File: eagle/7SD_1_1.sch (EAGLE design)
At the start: 16 parts, among them P1 7-SEG_SA56-11, X1 In A, X2 In B

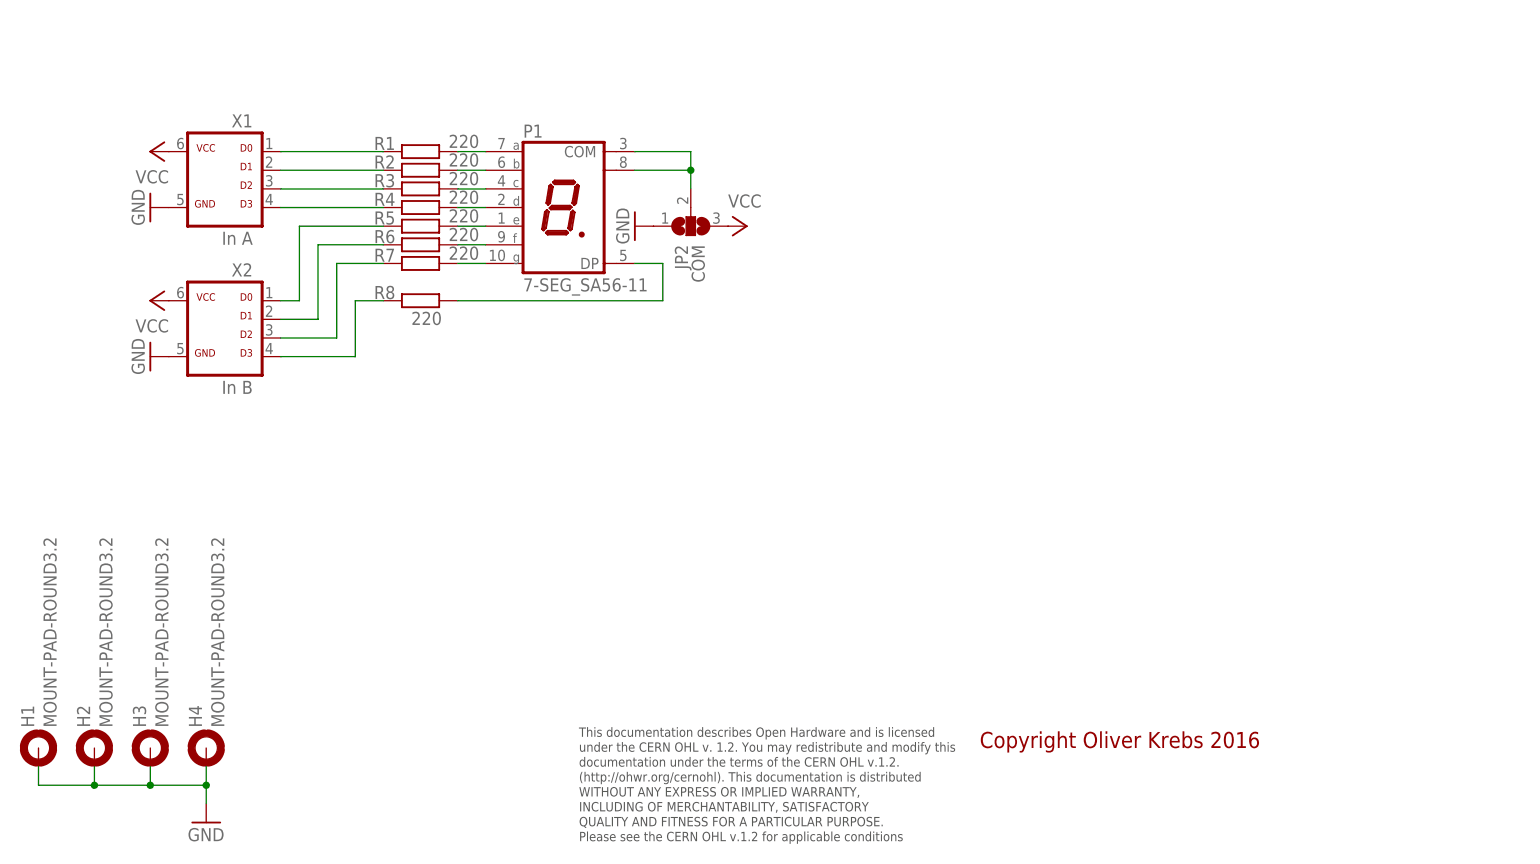
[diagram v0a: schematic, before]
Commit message: Add new tetra-Board and arduino files
Add AMP_1_0, AVC_1_0, D18_1_1, IOP_1_2, MIC_1_0, PIN_1_1, POT_1_0, PWA_1_0, PWR_1_0, RGF 2.0, SOC_2_0, VLT_1_0
Add mex_nano_shield_keyboard, mex_nano_shied_numbers

New arduino projects
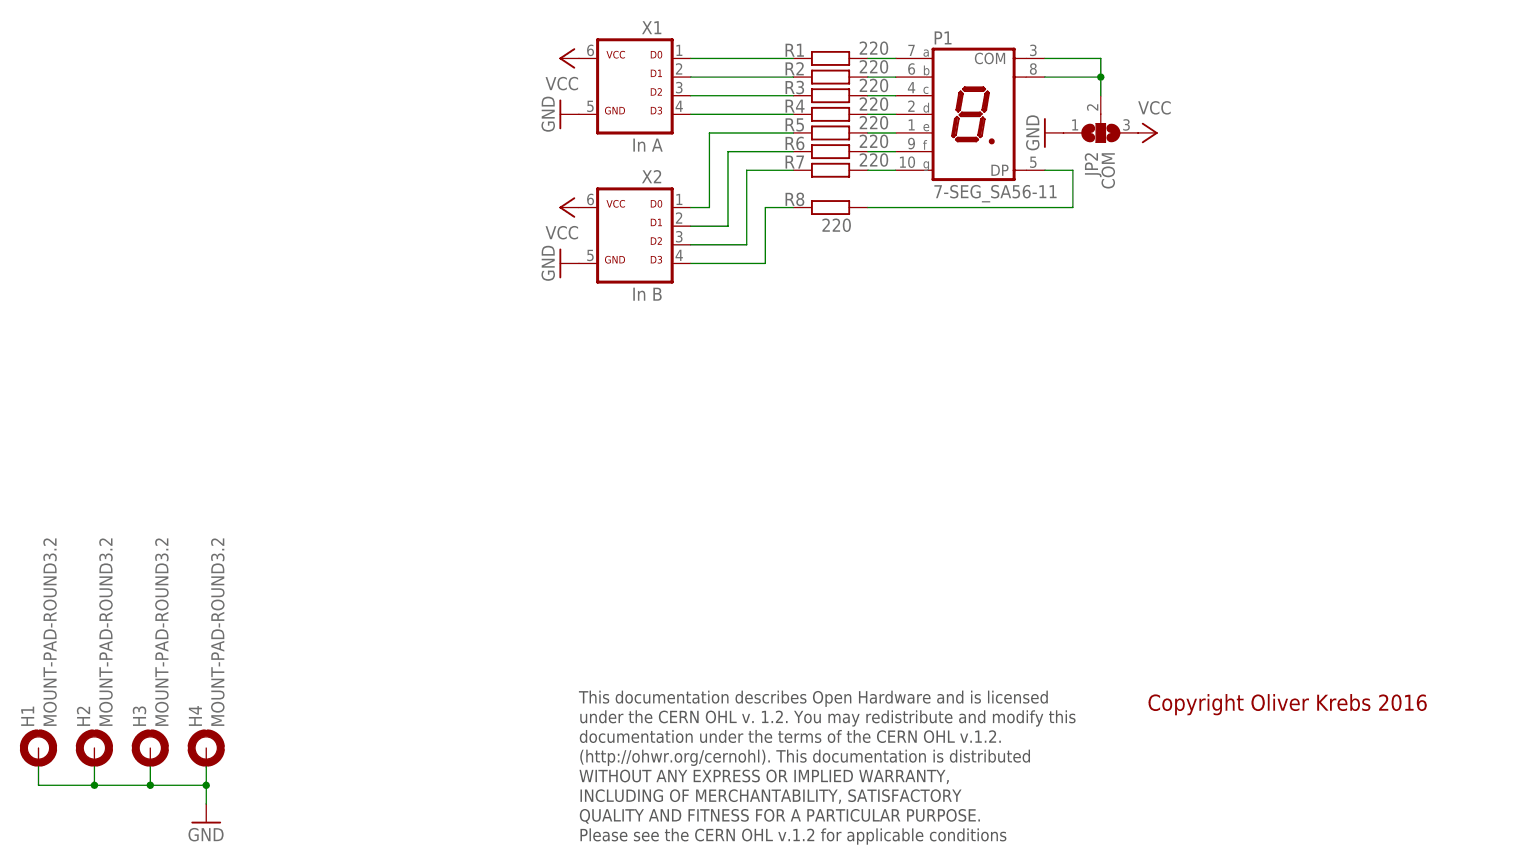
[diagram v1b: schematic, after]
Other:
- moved on the sheet: JP2, P1, R1, R2, R3, R4, R5, R6, R7, R8, X1, X2
